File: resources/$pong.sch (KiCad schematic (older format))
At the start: 23 parts, among them J1 RCA_JACK, J2 RCA_JACK, Q1 2N3904, SW1 SPST, SW2 left up, SW3 left down, SW4 right up, SW5 right down, U1 PIC10F322

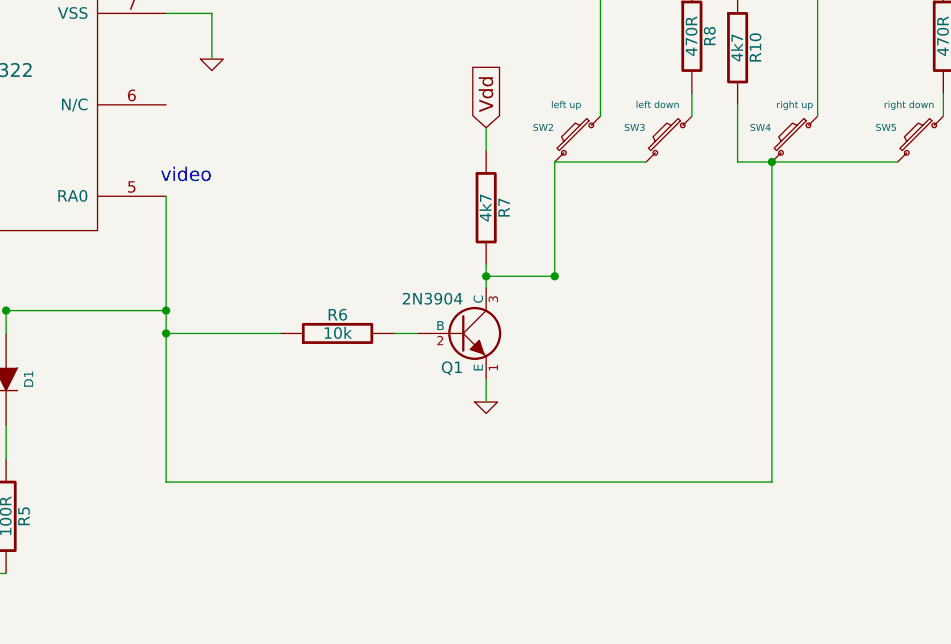
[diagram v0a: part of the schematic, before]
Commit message: modification chemin include du fichier pic10f322_m.inc dans mini-poing.asm
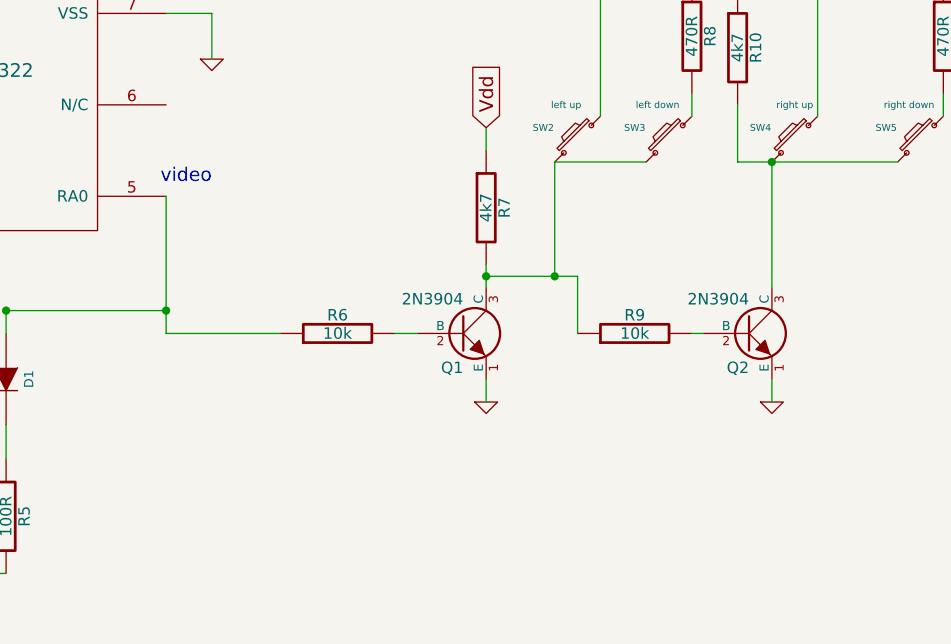
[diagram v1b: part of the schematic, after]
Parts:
- added Q2: 2N3904, symbol NPN
- added R9: 10k, symbol R
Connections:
- net GND: now also Q2.1 (E)
- net at D1.1 (A), R6.1, U1.5 (RA0): no longer R10.2, SW4.2, SW5.2
- net at Q1.3 (C), R7.2, SW2.2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: now also R9.1
- new net: Q2.2 (B), R9.2
- new net: Q2.3 (C), R10.2, SW4.2, SW5.2
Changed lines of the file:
@@
-EESchema Schematic File Version 2  date 2013-08-17 23:34:59
+EESchema Schematic File Version 2  date 2013-08-17 23:49:45
 LIBS:power
 LIBS:device
@@
 	1    0    0    -1
 $EndComp
-Wire Wire Line
-	4700 4250 4700 5100
-Wire Wire Line
-	5600 5300 5600 5450
-Wire Wire Line
-	4700 5600 4700 5950
-Wire Wire Line
-	4700 5950 5600 5950
-Wire Wire Line
-	4350 6450 4350 6550
-Wire Wire Line
-	3000 3900 3300 3900
-Wire Wire Line
-	6300 3500 6500 3500
-Wire Wire Line
-	6500 3500 6500 3700
-Wire Wire Line
-	3000 4400 3000 4500
-Connection ~ 2650 4400
-Wire Wire Line
-	4500 3500 4700 3500
-Wire Wire Line
-	1550 2250 1700 2250
-Wire Wire Line
-	2700 2000 2700 2350
-Connection ~ 2700 2250
-Wire Wire Line
-	2700 2250 3250 2250
-Wire Wire Line
-	3250 2250 3250 2350
-Wire Wire Line
-	3250 2750 3250 2950
-Wire Wire Line
-	2700 2750 2700 2950
-Wire Wire Line
-	1550 2850 1550 3000
-Wire Wire Line
-	5600 4900 5600 4800
-Connection ~ 5600 4800
-Connection ~ 4700 4600
 Text Notes 6500 4250 2    60   ~ 0
 video
@@
 Text Notes 6700 2500 2    197  ~ 0
 pong game
-Wire Wire Line
-	6300 4300 6300 5550
 Text GLabel 4000 3650 1    60   Input ~ 0
 RA2
-Wire Wire Line
-	4000 3900 4000 3650
-Connection ~ 4000 3900
-Wire Wire Line
-	3800 3900 4700 3900
-Connection ~ 3000 4400
-Connection ~ 3250 3900
 $Comp
 L NPN Q1
@@
 	0    -1   -1   0
 $EndComp
-Wire Wire Line
-	7700 5100 7700 5200
-Wire Wire Line
-	7300 4900 7400 4900
-Wire Wire Line
-	7700 4600 7700 4700
-Connection ~ 7700 4650
-Wire Wire Line
-	6300 4900 6800 4900
 Text GLabel 7700 4000 1    60   Input ~ 0
 Vdd
-Wire Wire Line
-	7700 4100 7700 4000
 $Comp
 L SW_PUSH_SMALL SW2
@@
 	-1   0    0    -1
 $EndComp
-Wire Wire Line
-	8950 4150 8950 5550
-Wire Wire Line
-	8800 4150 9500 4150
-Wire Wire Line
-	8400 4150 8000 4150
-Wire Wire Line
-	8000 4150 8000 4650
-Connection ~ 8000 4650
 $Comp
 L R R8
@@
 	1    0    0    -1
 $EndComp
-Wire Wire Line
-	8200 3150 8200 3950
-Wire Wire Line
-	9150 3150 9150 3950
 Text GLabel 7950 3350 0    60   Input ~ 0
 RA2
-Wire Wire Line
-	7950 3350 9700 3350
 $Comp
 L R R3
@@
 	1    0    0    -1
 $EndComp
-Wire Wire Line
-	3800 3900 3800 3800
 $Comp
 L R R10
@@
 	1    0    0    -1
 $EndComp
+Text GLabel 8800 2800 1    60   Input ~ 0
+Vdd
+Text GLabel 3800 3150 1    60   Input ~ 0
+Vdd
+Text Notes 7500 7550 0    60   ~ 0
+pong game\n
+Wire Wire Line
+	4700 4250 4700 5100
+Wire Wire Line
+	5600 5300 5600 5450
+Wire Wire Line
+	4700 5600 4700 5950
+Wire Wire Line
+	4700 5950 5600 5950
+Wire Wire Line
+	4350 6450 4350 6550
+Wire Wire Line
+	3000 3900 3300 3900
+Wire Wire Line
+	6300 3500 6500 3500
+Wire Wire Line
+	6500 3500 6500 3700
+Wire Wire Line
+	3000 4400 3000 4500
+Connection ~ 2650 4400
+Wire Wire Line
+	4500 3500 4700 3500
+Wire Wire Line
+	1550 2250 1700 2250
+Wire Wire Line
+	2700 2000 2700 2350
+Connection ~ 2700 2250
+Wire Wire Line
+	2700 2250 3250 2250
+Wire Wire Line
+	3250 2250 3250 2350
+Wire Wire Line
+	3250 2750 3250 2950
+Wire Wire Line
+	2700 2750 2700 2950
+Wire Wire Line
+	1550 2850 1550 3000
+Wire Wire Line
+	5600 4900 5600 4800
+Connection ~ 5600 4800
+Connection ~ 4700 4600
+Wire Wire Line
+	6300 4300 6300 4900
+Wire Wire Line
+	4000 3900 4000 3650
+Connection ~ 4000 3900
+Wire Wire Line
+	3800 3900 4700 3900
+Connection ~ 3000 4400
+Connection ~ 3250 3900
+Wire Wire Line
+	7700 5100 7700 5200
+Wire Wire Line
+	7300 4900 7400 4900
+Wire Wire Line
+	7700 4600 7700 4700
+Connection ~ 7700 4650
+Wire Wire Line
+	6300 4900 6800 4900
+Wire Wire Line
+	7700 4100 7700 4000
+Wire Wire Line
+	8950 4700 8950 4150
+Wire Wire Line
+	8800 4150 9500 4150
+Wire Wire Line
+	8400 4150 8000 4150
+Wire Wire Line
+	8000 4150 8000 4650
+Connection ~ 8000 4650
+Wire Wire Line
+	8200 3150 8200 3950
+Wire Wire Line
+	9150 3150 9150 3950
+Wire Wire Line
+	7950 3350 9700 3350
+Wire Wire Line
+	3800 3900 3800 3800
 Wire Wire Line
 	8800 3900 8800 4150
 Connection ~ 8950 4150
-Text GLabel 8800 2800 1    60   Input ~ 0
-Vdd
 Wire Wire Line
 	8800 2800 8800 3400
 Wire Wire Line
 	2650 4400 3000 4400
-Text GLabel 3800 3150 1    60   Input ~ 0
-Vdd
 Wire Wire Line
 	3800 3300 3800 3150
@@
 	5600 4800 6300 4800
 Connection ~ 6300 4800
-Text Notes 7500 7550 0    60   ~ 0
-pong game\n
 Wire Wire Line
 	6300 3150 9150 3150
@@
 	9700 3850 9700 3950
 Wire Wire Line
-	8000 4650 7700 4650
-Wire Wire Line
-	8950 5550 6300 5550
-Connection ~ 6300 4900
+	8100 4650 7700 4650
+Wire Wire Line
+	8100 4900 8100 4650
+Wire Wire Line
+	8600 4900 8650 4900
+$Comp
+L R R9
+U 1 1 520CE635
+P 8350 4900
+F 0 "R9" V 8430 4900 50  0000 C CNN
+F 1 "10k" V 8350 4900 50  0000 C CNN
+F 2 "" H 8350 4900 60  0000 C CNN
+F 3 "" H 8350 4900 60  0000 C CNN
+	1    8350 4900
+	0    -1   -1   0
+$EndComp
+$Comp
+L GND #PWR8
+U 1 1 520CE604
+P 8950 5200
+F 0 "#PWR8" H 8950 5200 30  0001 C CNN
+F 1 "GND" H 8950 5130 30  0001 C CNN
+F 2 "" H 8950 5200 60  0000 C CNN
+F 3 "" H 8950 5200 60  0000 C CNN
+	1    8950 5200
+	1    0    0    -1
+$EndComp
+Wire Wire Line
+	8950 5100 8950 5200
+$Comp
+L NPN Q2
+U 1 1 520CE5F4
+P 8850 4900
+F 0 "Q2" H 8850 4750 50  0000 R CNN
+F 1 "2N3904" H 8850 5050 50  0000 R CNN
+F 2 "" H 8850 4900 60  0000 C CNN
+F 3 "" H 8850 4900 60  0000 C CNN
+	1    8850 4900
+	1    0    0    -1
+$EndComp
 $EndSCHEMATC
